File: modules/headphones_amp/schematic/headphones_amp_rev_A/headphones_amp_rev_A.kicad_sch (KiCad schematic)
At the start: 100 parts, among them J1 AudioJack3_SwitchTR, J2 AudioJack3_SwitchTR, J3 Conn_01x02, J4 Conn_01x02, J5 Conn_01x02, Q1 BC140, Q10 BC548, Q11 BC548, Q12 BC140, Q13 BC160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

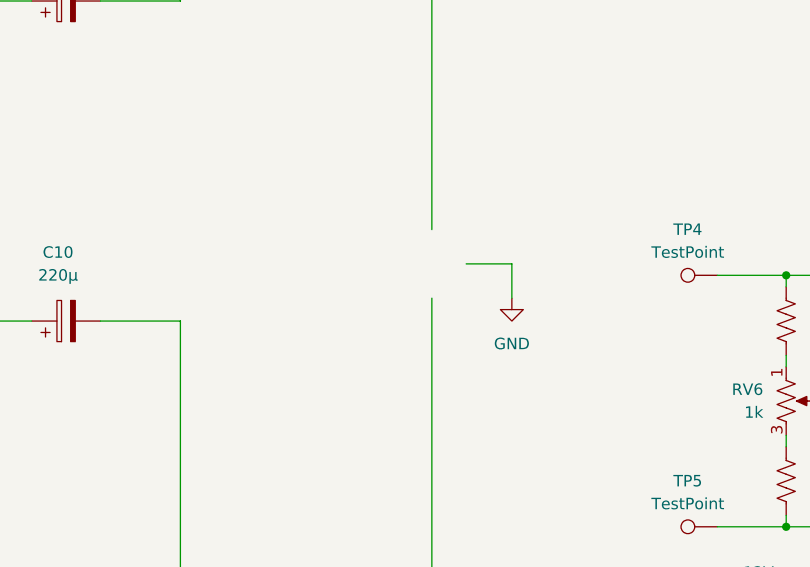
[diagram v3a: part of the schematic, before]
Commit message: added outline for the PCB
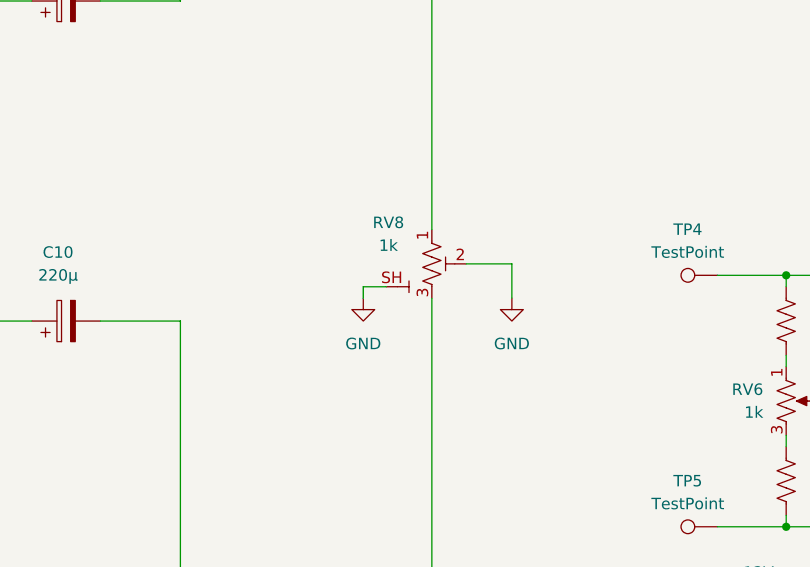
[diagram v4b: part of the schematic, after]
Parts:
- added RV8: 1k, ProjectLib_Transient:Potentiometer_Bourns_PTV09A-4_Single_Vertical, symbol ProjectLib_Transient:R_Potentiometer_Shield_US
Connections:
- net GND: now also RV8.2 (W), RV8.SH
- net at C6.1, R44.1: now also RV8.3 (B)
- net at R21.2: now also RV8.1 (A)
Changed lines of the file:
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@@
 	(wire
 		(pts
+			(xy 127 180.34) (xy 127 181.61)
+		)
+		(stroke
+			(width 0)
+			(type default)
+		)
+	)
+	(wire
+		(pts
 			(xy 287.02 111.76) (xy 303.53 111.76)
 		)
@@
 	(wire
 		(pts
+			(xy 129.54 180.34) (xy 127 180.34)
+		)
+		(stroke
+			(width 0)
+			(type default)
+		)
+	)
+	(wire
+		(pts
 			(xy 303.53 179.07) (xy 331.47 179.07)
 		)
@@
 	)
 	(symbol
+		(lib_id "ProjectLib_Transient:R_Potentiometer_Shield_US")
+		(at 134.62 177.8 0)
+		(unit 1)
+		(exclude_from_sim no)
+		(in_bom yes)
+		(on_board yes)
+		(dnp no)
+		(property "Reference" "RV8"
+			(at 129.794 173.228 0)
+			(effects
+				(font
+					(size 1.27 1.27)
+				)
+			)
+		)
+		(property "Value" "1k"
+			(at 129.794 175.768 0)
+			(effects
+				(font
+					(size 1.27 1.27)
+				)
+			)
+		)
+		(property "Footprint" "ProjectLib_Transient:Potentiometer_Bourns_PTV09A-4_Single_Vertical"
+			(at 134.874 196.85 0)
+			(effects
+				(font
+					(size 1.27 1.27)
+				)
+				(hide yes)
+			)
+		)
+		(property "Datasheet" "~"
+			(at 134.62 177.8 0)
+			(effects
+				(font
+					(size 1.27 1.27)
+				)
+				(hide yes)
+			)
+		)
+		(property "Description" "Dual potentiometer (US symbol) with shield connection"
+			(at 141.224 164.592 0)
+			(effects
+				(font
+					(size 1.27 1.27)
+				)
+				(hide yes)
+			)
+		)
+		(pin "2"
+		)
+		(pin "SH"
+		)
+		(pin "1"
+		)
+		(pin "3"
+		)
+		(instances
+			(project ""
+				(path "/d2365754-669a-45b0-8c88-535b259ec7b7"
+					(reference "RV8")
+					(unit 1)
+				)
+			)
+		)
+	)
+	(symbol
 		(lib_id "power:+12V")
 		(at 331.47 175.26 0)
@@
 				)
 			)
+		)
+	)
+	(symbol
+		(lib_id "power:GND")
+		(at 127 181.61 0)
+		(unit 1)
+		(exclude_from_sim no)
+		(in_bom yes)
+		(on_board yes)
+		(dnp no)
+		(fields_autoplaced yes)
+		(property "Reference" "#PWR040"
+			(at 127 187.96 0)
+			(effects
+				(font
+					(size 1.27 1.27)
+				)
+				(hide yes)
+			)
+		)
+		(property "Value" "GND"
+			(at 127 186.69 0)
+			(effects
+				(font
+					(size 1.27 1.27)
+				)
+			)
+		)
+		(property "Footprint" ""
+			(at 127 181.61 0)
+			(effects
+				(font
+					(size 1.27 1.27)
+				)
+				(hide yes)
+			)
+		)
+		(property "Datasheet" ""
+			(at 127 181.61 0)
+			(effects
+				(font
+					(size 1.27 1.27)
+				)
+				(hide yes)
+			)
+		)
+		(property "Description" "Power symbol creates a global label with name \"GND\" , ground"
+			(at 127 181.61 0)
+			(effects
+				(font
+					(size 1.27 1.27)
+				)
+				(hide yes)
+			)
+		)
+		(pin "1"
+		)
+		(instances
+			(project "headphones_amp_rev_A"
+				(path "/d2365754-669a-45b0-8c88-535b259ec7b7"
+					(reference "#PWR040")
+					(unit 1)
+				)
+			)

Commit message: updated the pcb outline
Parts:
- added J6, J7: Conn_01x02, ProjectLib_Transient:WuerthElectronik_WR_TBL_Series_2109_1x02_P2.54mm_Horizontal, symbol Connector_Generic:Conn_01x02
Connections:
- net GND: now also J2.S, J6.2 (Pin_2), J7.2 (Pin_2)
- net out_L: now also J6.1 (Pin_1)
- net out_R: now also J7.1 (Pin_1)
- net at J2.R: now also J1.RN
- net at J2.T: now also J1.TN
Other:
- moved on the sheet: C4, C5, D1, H1, H2, H3, H4, J1, J2, J5, R25, SW1

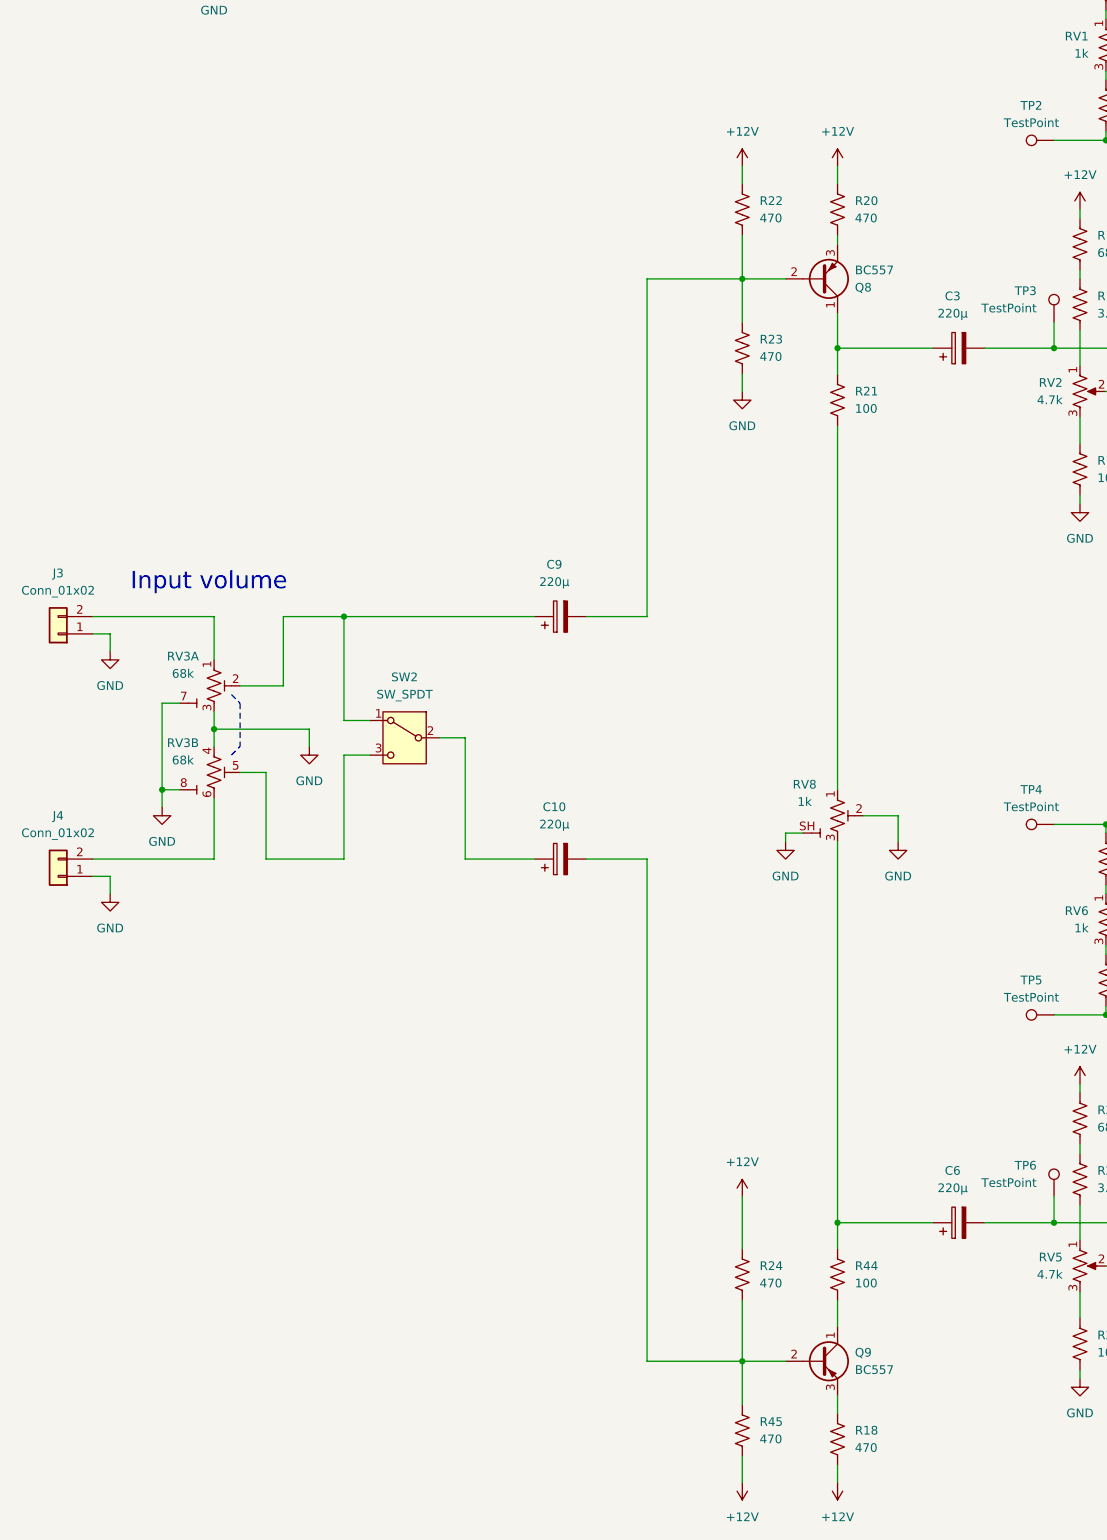
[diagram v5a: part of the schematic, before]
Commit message: - added a bootstrap structure for improved input impedance - moved the mono/stereo junction point
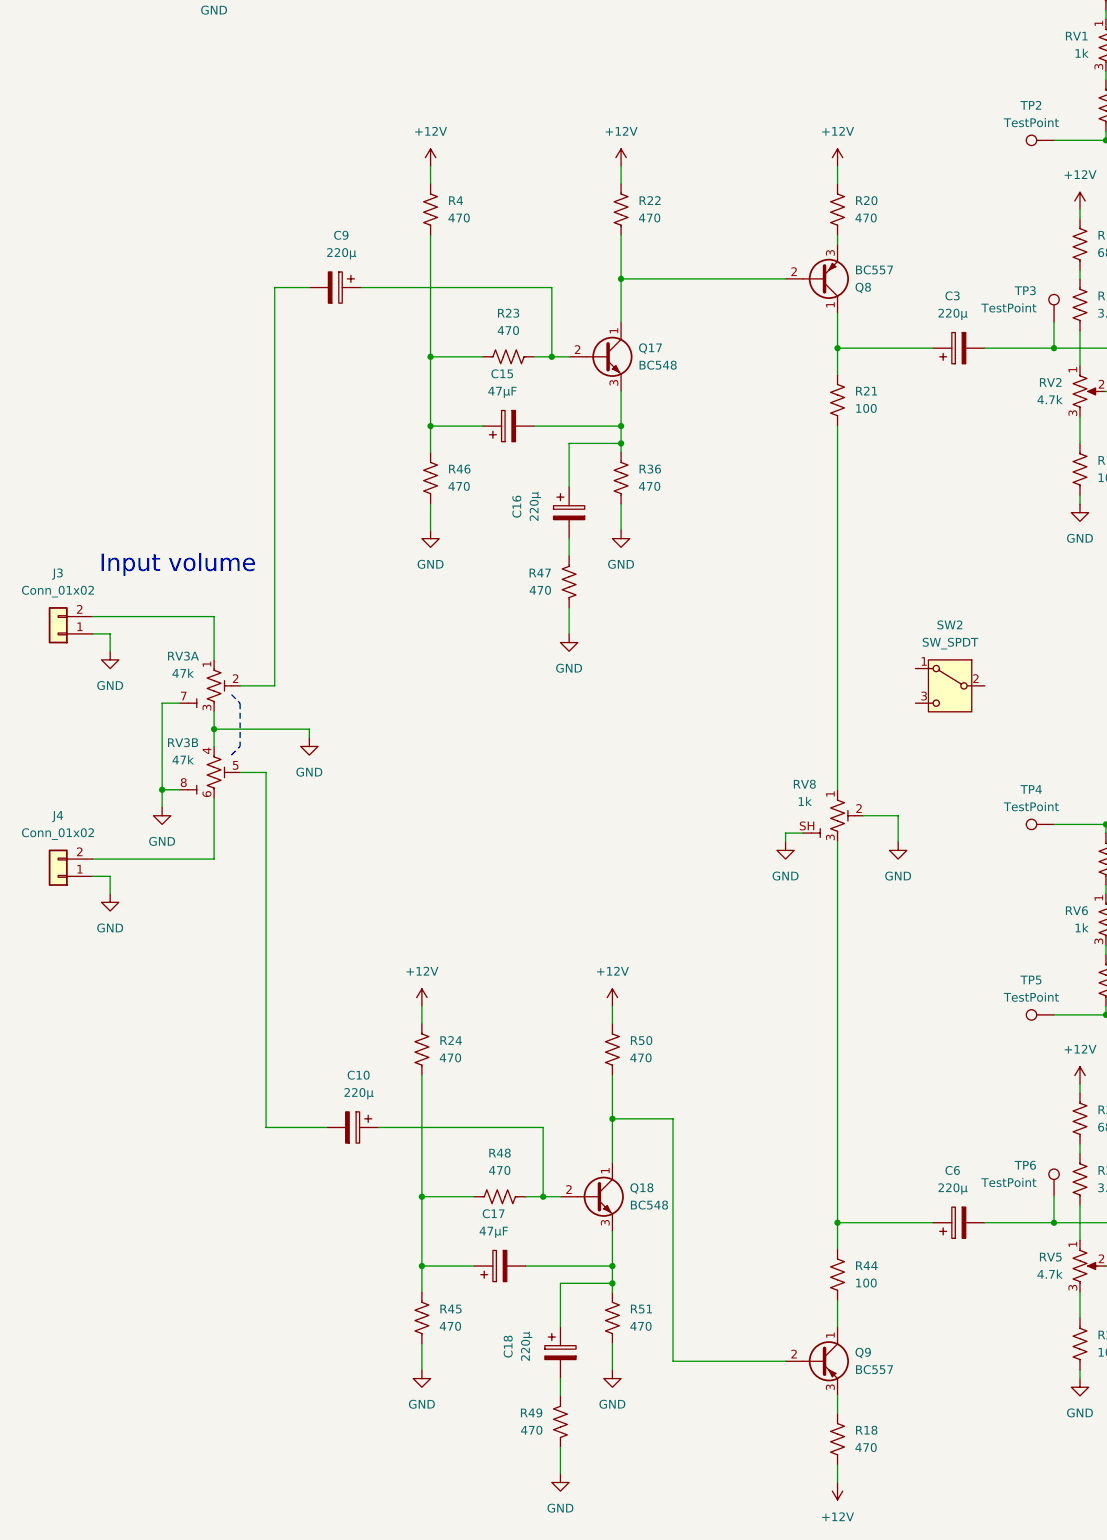
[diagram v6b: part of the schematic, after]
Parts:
- added C15, C17: 47µF, Capacitor_THT:CP_Radial_D10.0mm_P5.00mm, symbol Device:C_Polarized
- added C16, C18: 220µ, Capacitor_THT:CP_Radial_D10.0mm_P5.00mm, symbol Device:C_Polarized
- added Q17, Q18: BC548, Package_TO_SOT_THT:TO-92L_Inline_Wide, symbol Transistor_BJT:BC548
- added R36, R4, R46, R47, R48, R49, R50, R51: 470, Resistor_THT:R_Axial_DIN0207_L6.3mm_D2.5mm_P10.16mm_Horizontal, symbol Device:R_US
- RV3: value 68k -> 47k
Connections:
- net +12V: now also R4.1, R50.1; no longer R45.2
- net GND: now also R45.2, R36.2, R46.2, R47.2, R49.2, R51.2; no longer R23.2
- net at R24.2, R45.1: now also C17.1, R48.1; no longer C10.2, Q9.2 (B)
- net at Q8.2 (B), R22.2: now also Q17.1 (C); no longer C9.2, R23.1
- net at C10.1: now also Q18.2 (B), R48.2; no longer SW2.2
- net at RV3.5 (W): now also C10.2; no longer SW2.3
- new net: C18.2, R49.1
- new net: C15.2, C16.1, Q17.3 (E), R36.1
- new net: C16.2, R47.1
- new net: C15.1, R23.1, R4.2, R46.1
- new net: Q18.1 (C), Q9.2 (B), R50.2
- new net: C17.2, C18.1, Q18.3 (E), R51.1
- new net: C9.1, Q17.2 (B), R23.2
- new net: C9.2, RV3.2 (W)
- now unconnected: SW2.1
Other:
- moved on the sheet: C10, C9, R22, SW2

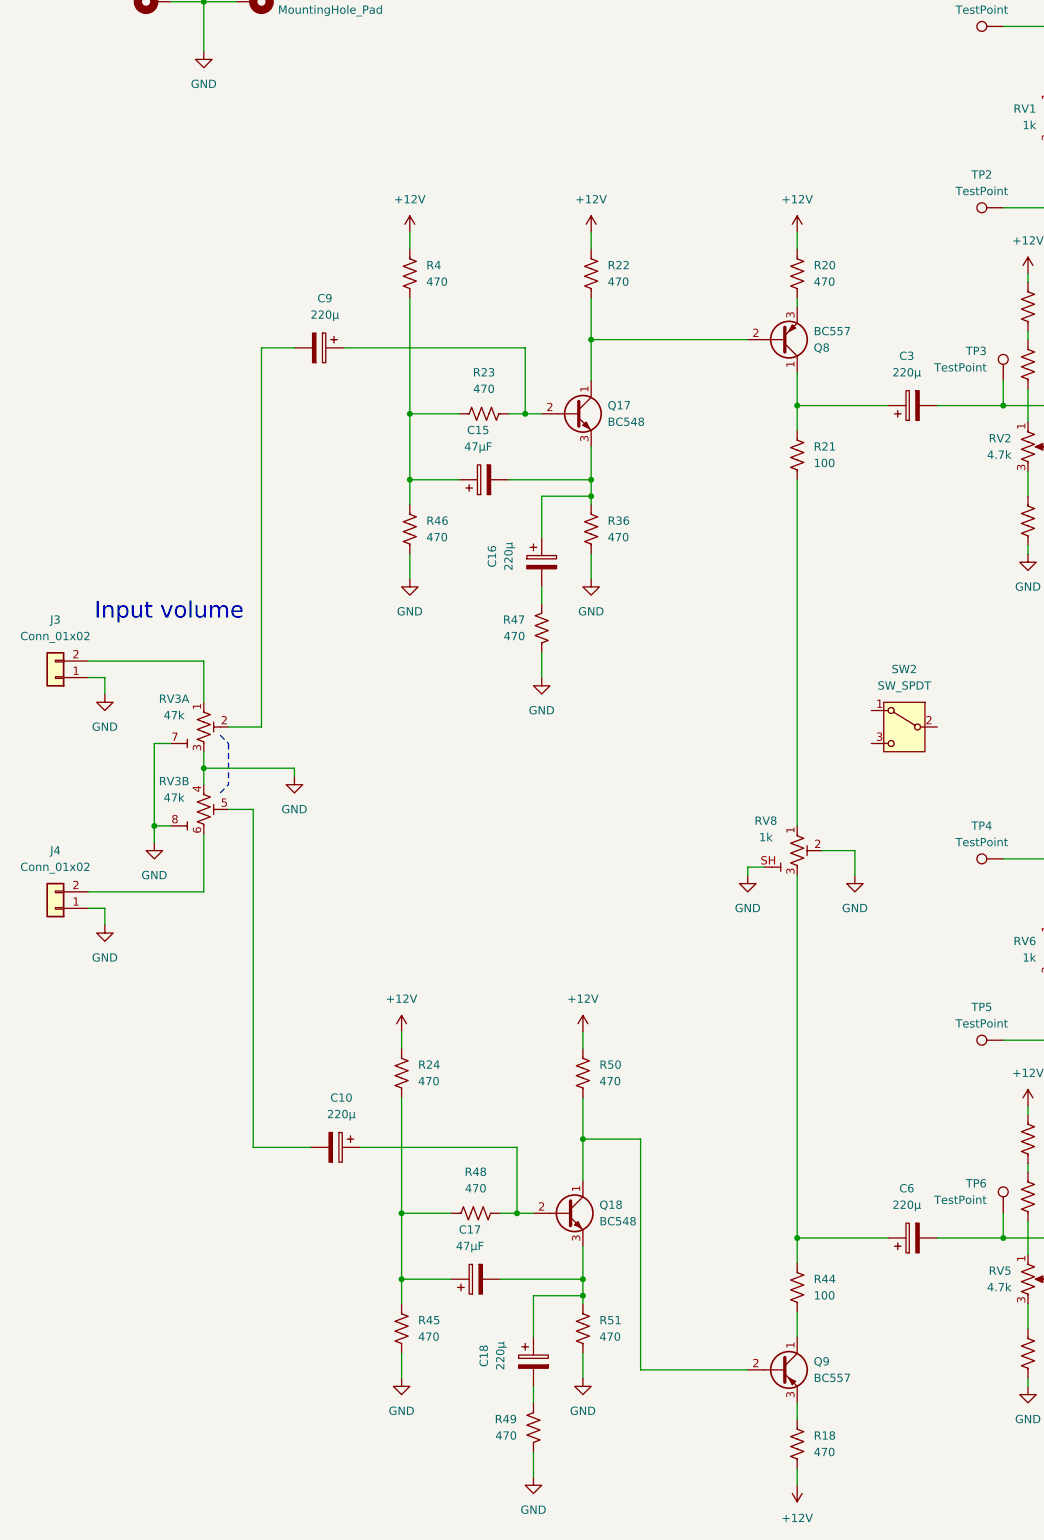
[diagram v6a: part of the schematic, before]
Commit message: input stage: improved biasing (more stable version), added component values (validated on prototype) PCB cleanup (useless footprints)
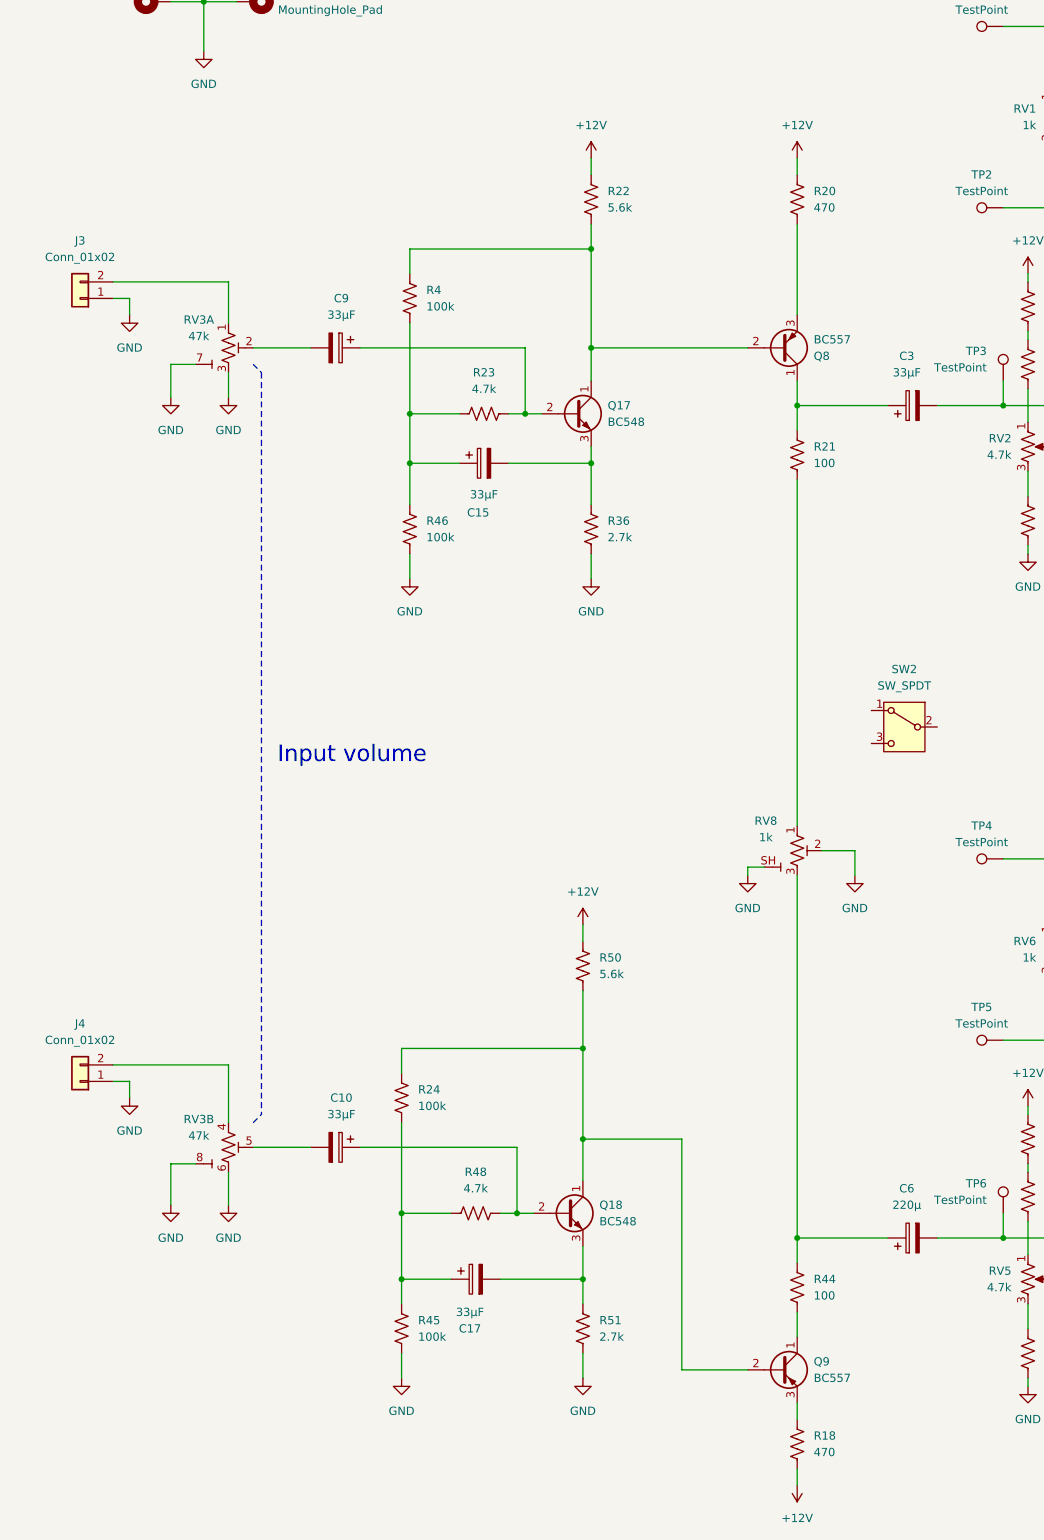
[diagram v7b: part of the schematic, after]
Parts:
- removed C16, C18: 220µ, Capacitor_THT:CP_Radial_D10.0mm_P5.00mm, symbol Device:C_Polarized
- removed R47, R49: 470, Resistor_THT:R_Axial_DIN0207_L6.3mm_D2.5mm_P10.16mm_Horizontal, symbol Device:R_US
- C10, C3, C9: value 220µ -> 33µF
- C15, C17: value 47µF -> 33µF
- R22, R50: value 470 -> 5.6k
- R23, R48: value 470 -> 4.7k
- R24, R4, R45, R46: value 470 -> 100k
- R36, R51: value 470 -> 2.7k
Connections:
- net +12V: no longer R24.1, R4.1
- net GND: now also RV3.6 (B); no longer RV3.4 (A)
- net at Q18.1 (C), Q9.2 (B), R50.2: now also R24.1
- net at Q17.1 (C), Q8.2 (B), R22.2: now also R4.1
- net at J4.2 (Pin_2): now also RV3.4 (A); no longer RV3.6 (B)
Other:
- moved on the sheet: C15, C9, J3, J4, Q8, R20, R22, R24, R4, R50, RV3A, RV3B

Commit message: PCB progress backup All parts finally fit in the board!
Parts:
- C6: value 220µ -> 33µF
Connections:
- net at R44.1, RV8.3 (B): now also SW2.3; no longer C6.1
- net at C3.1, Q8.1 (C), R21.1: now also SW2.1
- net at SW2.2: now also C6.1
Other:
- moved on the sheet: C13, C14, C3, C6, C7, J1, J2, J6, J7, Q10, Q11, Q12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
